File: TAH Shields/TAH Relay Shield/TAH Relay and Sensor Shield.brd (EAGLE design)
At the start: 86.8 x 54 mm, 40 parts, among them T1 2N3904, T2 2N3904

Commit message: TAH Shields new version update
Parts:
- removed U$4, U$5: (no value), TAH:TAHLOGO
- added U$2: (no value), TAH:TAHLOGO
- moved D3 2.10 mm to (10.0, 14.1)
- moved IC1 2.10 mm to (19.0, 14.1)
- moved U$1 0.14 mm to (19.1, 5.46), flipped to the bottom
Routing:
- net A4: track 140.3 -> 70.3 mm, vias 2 -> 0
- net D3: track 11.8 -> 80.2 mm, vias 0 -> 2
- net D4: track 53.2 -> 113.2 mm, vias 1 -> 2
- net D6: track 32.9 -> 91.4 mm
- net D10: track 50.1 -> 108.1 mm, vias 2 -> 1
- net D2: track 9.23 -> 64.7 mm, vias 0 -> 2
- net D7: track 20.9 -> 75.9 mm
- net D5: track 59.6 -> 98.1 mm, vias 1 -> 2
- net A5: track 52.5 -> 83.0 mm, vias 2 -> 1
- net A0: track 46.6 -> 21.2 mm, vias 1 -> 0
- net D8: track 14.2 -> 39.0 mm
- net N$5: track 43.2 -> 64.3 mm, vias 1 -> 5
- net A2: track 33.8 -> 54.2 mm, vias 2 -> 0
- net A1: track 61.3 -> 43.3 mm, vias 3 -> 0
- net 5V: track 212.4 -> 200.0 mm, vias 2 -> 0
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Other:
- board text added: "http://www.tah.io/start"
- board text removed: "by Revealing Hour Creations"

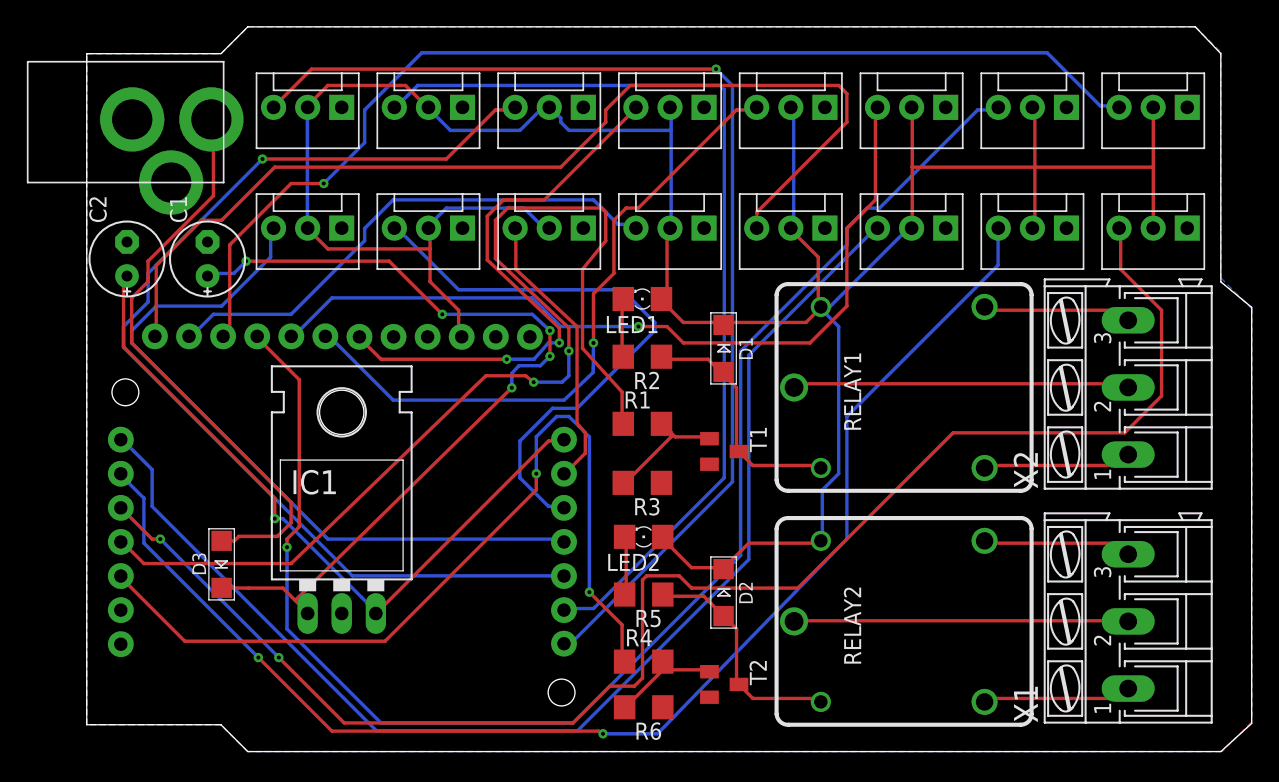
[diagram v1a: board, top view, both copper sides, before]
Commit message: All shields updated with latest Tah footprint
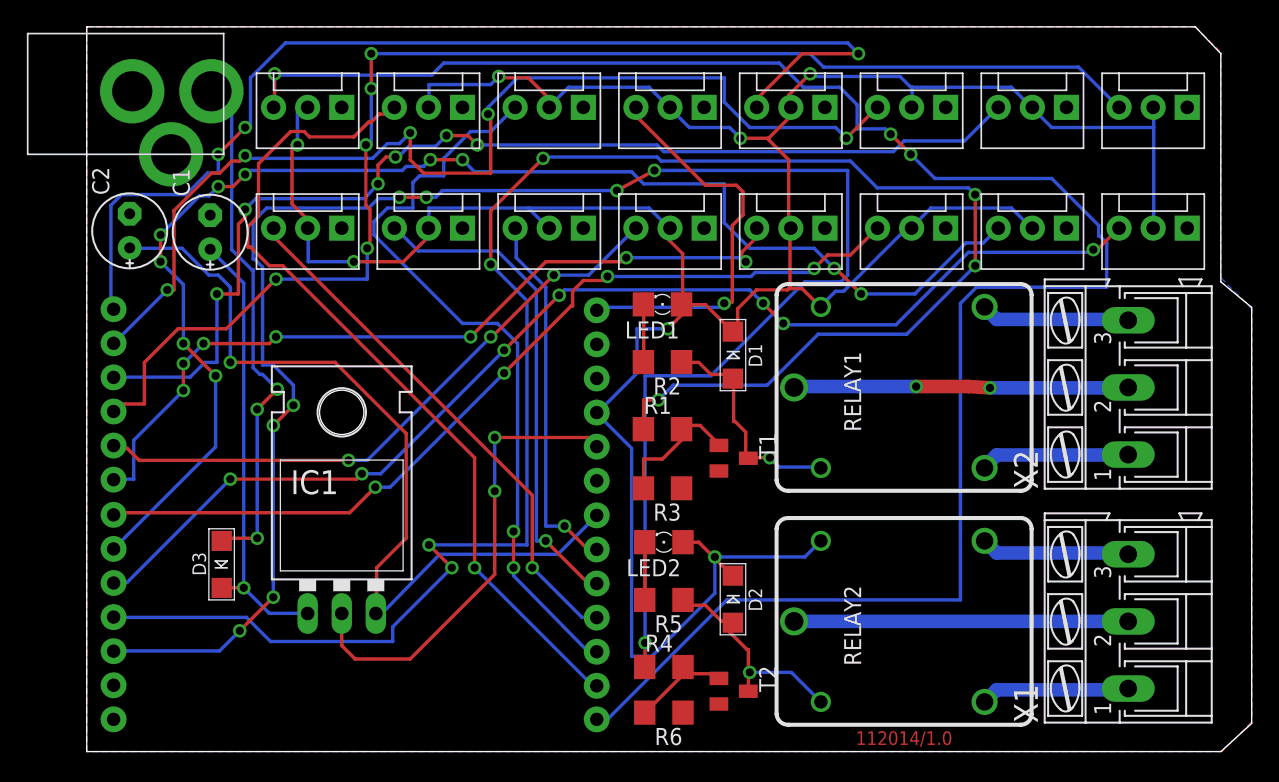
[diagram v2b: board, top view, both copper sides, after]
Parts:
- added U$4: (no value), TAH:TAH_PIN_FOOTPRINT_WITHOUT_ICSP_VERS1.0_SILK
- moved U$2 17.7 mm to (61.0, 12.1)
- moved U$1 10.5 mm to (20.4, 15.8)
- moved C2 2.11 mm to (3.20, 38.8)
- moved U$3 2.10 mm to (0.00, 49.1)
- moved C1 2.01 mm to (9.20, 38.7)
- moved R1 1.55 mm to (42.9, 24.0)
- moved R2 1.55 mm to (42.9, 29.0)
- moved LED2 1.55 mm to (43.0, 15.6)
- moved R4 1.55 mm to (43.0, 6.30)
- moved R6 1.55 mm to (43.0, 2.90)
- moved LED1 1.55 mm to (42.9, 33.3)
- moved R3 1.55 mm to (42.9, 19.6)
- moved R5 1.55 mm to (43.0, 11.3)
- moved D1 0.86 mm to (48.2, 29.4)
- moved D2 0.86 mm to (48.2, 11.2)
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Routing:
- net D2: track 64.7 -> 137.3 mm, vias 2 -> 9
- net D3: track 80.2 -> 139.9 mm, vias 2 -> 7
- net A5: track 83.0 -> 139.7 mm, vias 1 -> 3
- net GND: track 0.58 -> 34.9 mm, vias 0 -> 2
- net D12: track 48.9 -> 81.7 mm, vias 1 -> 3
- net N$5: track 64.3 -> 33.5 mm, vias 5 -> 1
- net 5V: track 200.0 -> 229.3 mm, vias 0 -> 7
- net D10: track 108.1 -> 82.5 mm, vias 1 -> 6
- net D4: track 113.2 -> 88.0 mm, vias 2 -> 7
- net D6: track 91.4 -> 66.4 mm, vias 0 -> 4
- net A3: track 78.6 -> 57.2 mm, vias 1 -> 2
- net D11: track 60.8 -> 79.5 mm, vias 1 -> 5
- net D9: track 82.3 -> 99.7 mm, vias 1 -> 5
- net D7: track 75.9 -> 60.3 mm, vias 0 -> 7
- net A2: track 54.2 -> 39.7 mm, vias 0 -> 1
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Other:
- outline, holes or cut-outs redrawn
- board text added: "112014/1.0"
- board text added: "http://tah.io/start"
- board text removed: "http://www.tah.io/start"

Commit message: Silk Screen related minor changes
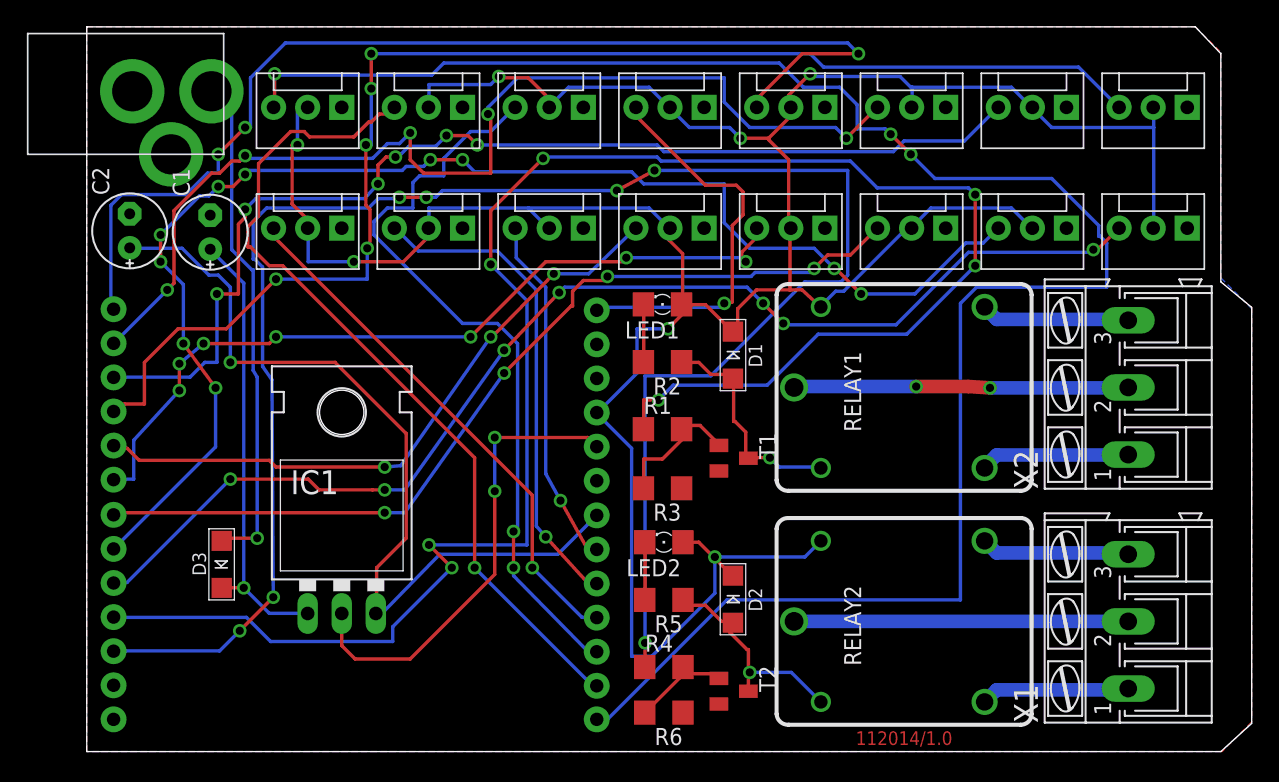
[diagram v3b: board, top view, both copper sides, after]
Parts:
- U$1: device TAH:TAH_PIN_FOOTPRINT_WITHOUT_ICSP_VER1.0 -> TAH:FOOTPRINT_WITHOUT_ICSP
- U$4: device TAH:TAH_PIN_FOOTPRINT_WITHOUT_ICSP_VERS1.0_SILK -> TAH:TAH_SILK_FLIPPED
- moved U$4 0.51 mm to (20.6, 17.7)
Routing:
- net D4: track 88.0 -> 90.0 mm
- net D2: track 137.3 -> 135.5 mm, vias 9 -> 7
- net D8: track 46.5 -> 47.9 mm
- net N$4: track 39.7 -> 38.3 mm, vias 3 -> 1
- net A0: track 27.7 -> 26.4 mm
- net D6: track 66.4 -> 67.5 mm
- net A1: track 37.0 -> 36.5 mm

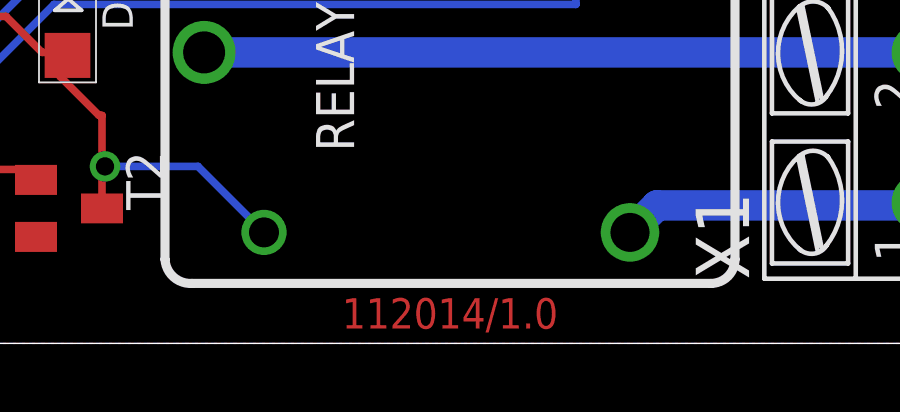
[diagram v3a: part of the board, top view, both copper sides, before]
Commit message: Updated production ready files for Tah and shields
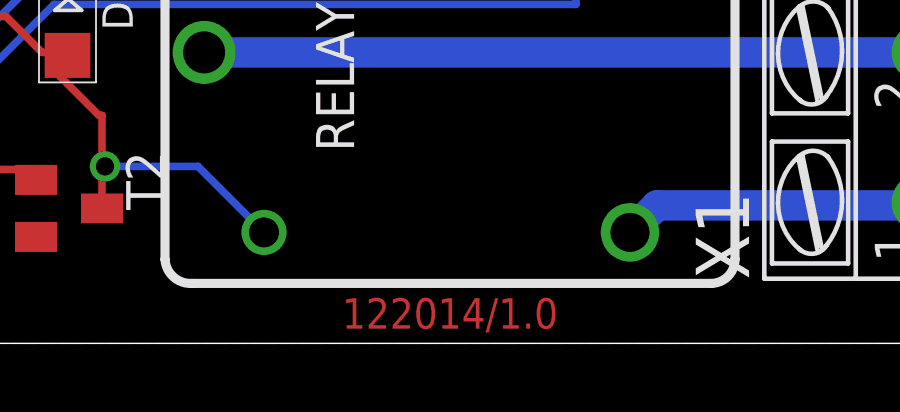
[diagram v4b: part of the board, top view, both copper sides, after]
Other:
- board text added: "122014/1.0"
- board text removed: "112014/1.0"
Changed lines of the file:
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@@
 <text x="61" y="8.8" size="1.016" layer="22" rot="MR0" align="center">Made In India</text>
 <text x="61" y="7.1" size="1.016" layer="22" rot="MR0" align="center">http://tah.io/start</text>
-<text x="60.9" y="1" size="1.016" layer="1" align="center">112014/1.0</text>
+<text x="60.9" y="1" size="1.016" layer="1" align="center">122014/1.0</text>
 </plain>
 <attributes>

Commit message: updated board files
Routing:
- net GND: track 34.9 -> 43.9 mm
- net A4: track 63.1 -> 62.8 mm, vias 1 -> 3
